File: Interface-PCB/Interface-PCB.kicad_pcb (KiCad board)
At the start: 2 copper layers, 36 parts, among them IC1 SN74LVC245AN, J10 LEVEL_SENSOR, J11 LEVEL_SENSOR, J12 LEVEL_SENSOR, J13 TEMPERATURE_SENSOR, J14 TEMPERATURE_SENSOR, J3 RASPBERRYPI-40-PIN-GPIO, J4 I2C_HEADER, J5 CONN_05JST, J6 CONN_05JST, J7 LEVEL_SENSOR, J8 LEVEL_SENSOR, J9 LEVEL_SENSOR, Q1 2N3904, Q10 2N3904, Q2 2N3904, Q3 2N3904, Q4 2N3904, Q5 2N3904, Q6 2N3904, Q7 2N3904, Q8 2N3904, Q9 2N3904, U3 CD74HC4067_MUX

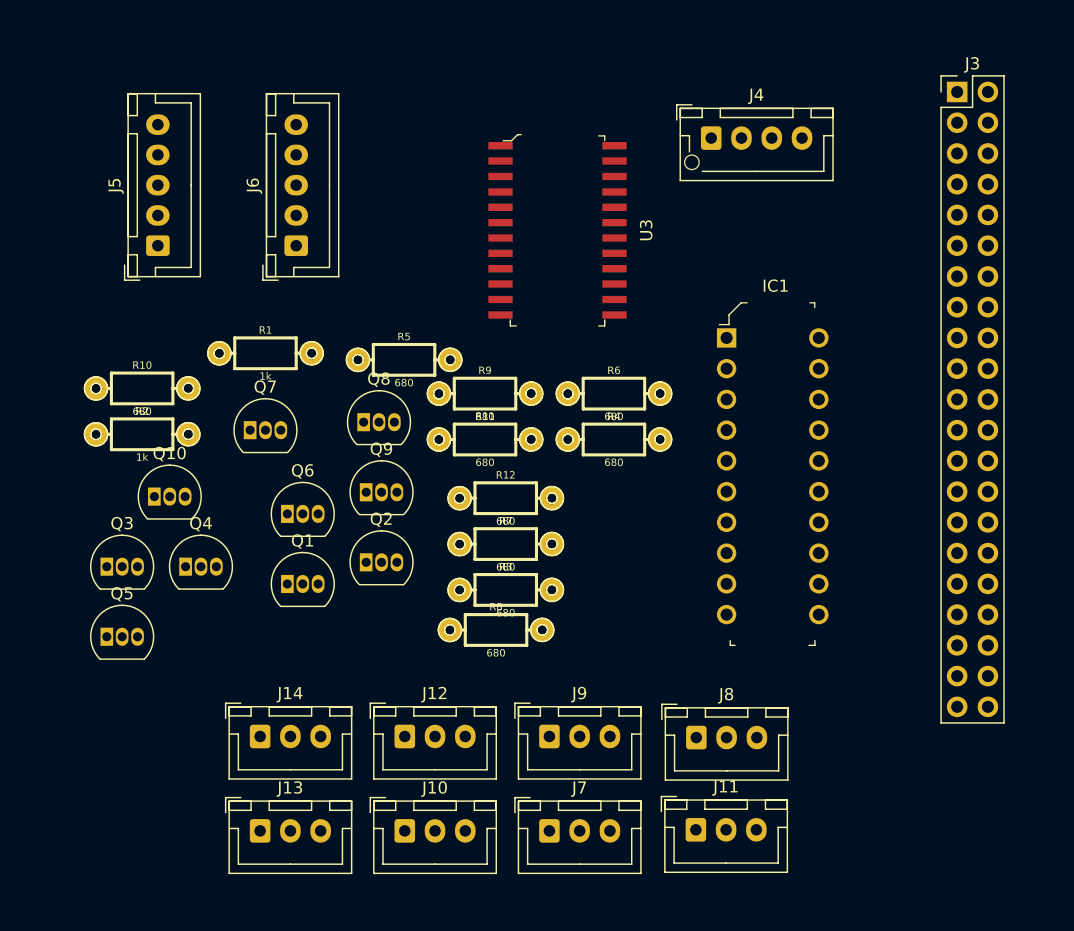
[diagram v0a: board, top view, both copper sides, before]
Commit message: Assign misc footprints for FDP
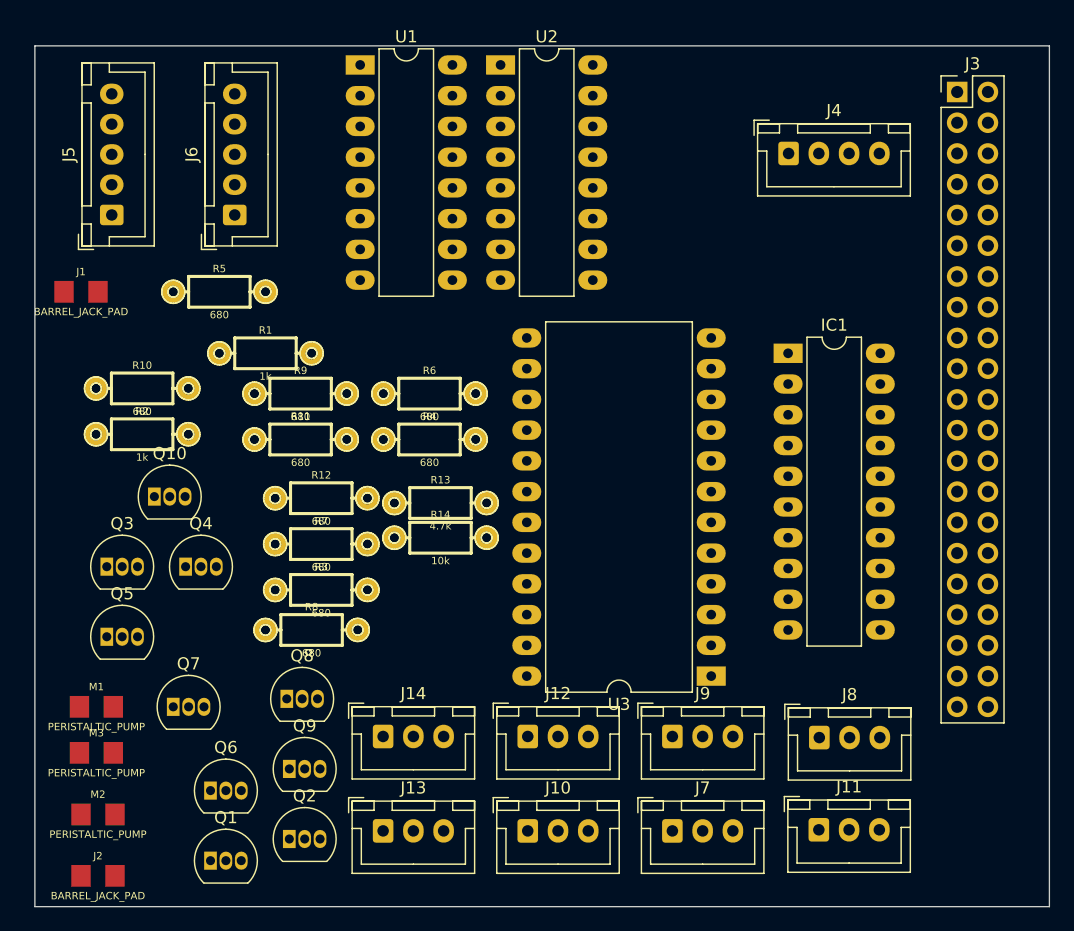
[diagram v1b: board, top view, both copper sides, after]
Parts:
- added J1: BARREL_JACK_PAD, Fuses:1206, F.Cu at (125.7, 95.2)
- added J2: BARREL_JACK_PAD, Fuses:1206, F.Cu at (127.1, 143.5)
- added M1: PERISTALTIC_PUMP, Fuses:1206, F.Cu at (127.0, 129.5)
- added M2: PERISTALTIC_PUMP, Fuses:1206, F.Cu at (127.1, 138.4)
- added M3: PERISTALTIC_PUMP, Fuses:1206, F.Cu at (127.0, 133.3)
- added R13: 4.7k, Resistors:AXIAL-0.3-KIT, F.Cu at (155.4, 112.7)
- added R14: 10k, Resistors:AXIAL-0.3-KIT, F.Cu at (155.4, 115.6)
- added U1: TB6612FNG_BREAKOUT, Package_DIP:DIP-16_W7.62mm_LongPads, F.Cu at (148.8, 76.5)
- added U2: TB6612FNG_BREAKOUT, Package_DIP:DIP-16_W7.62mm_LongPads, F.Cu at (160.4, 76.5)
- IC1: footprint digikey-footprints:DIP-20_W7.62mm -> Package_DIP:DIP-20_W7.62mm_LongPads
- J4: footprint Connector_JST:JST_XH_B4B-XH-AM_1x04_P2.50mm_Vertical -> Connector_JST:JST_XH_B4B-XH-A_1x04_P2.50mm_Vertical
- U3: footprint digikey-footprints:SOIC-24_W7.50mm -> Package_DIP:DIP-24_W15.24mm_LongPads
- moved U3 39.0 mm to (177.8, 127.0), turned to 180 degrees
- moved Q2 23.7 mm to (142.9, 140.5)
- moved Q6 23.7 mm to (136.4, 136.5)
- moved Q8 23.7 mm to (142.7, 128.9)
- moved Q1 23.7 mm to (136.4, 142.2)
- moved Q7 23.7 mm to (133.3, 129.5)
- moved Q9 23.7 mm to (142.9, 134.7)
- moved R5 16.3 mm to (137.2, 95.2)
- moved R12 15.2 mm to (145.6, 112.3)
- moved R3 15.2 mm to (145.6, 119.9)
- moved R4 15.2 mm to (154.5, 107.5)
- moved R6 15.2 mm to (154.5, 103.7)
- moved R7 15.2 mm to (145.6, 116.1)
- moved R8 15.2 mm to (144.8, 123.2)
- moved R11 15.2 mm to (143.9, 107.5)
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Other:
- board outline added: 83.8 x 71.1 mm

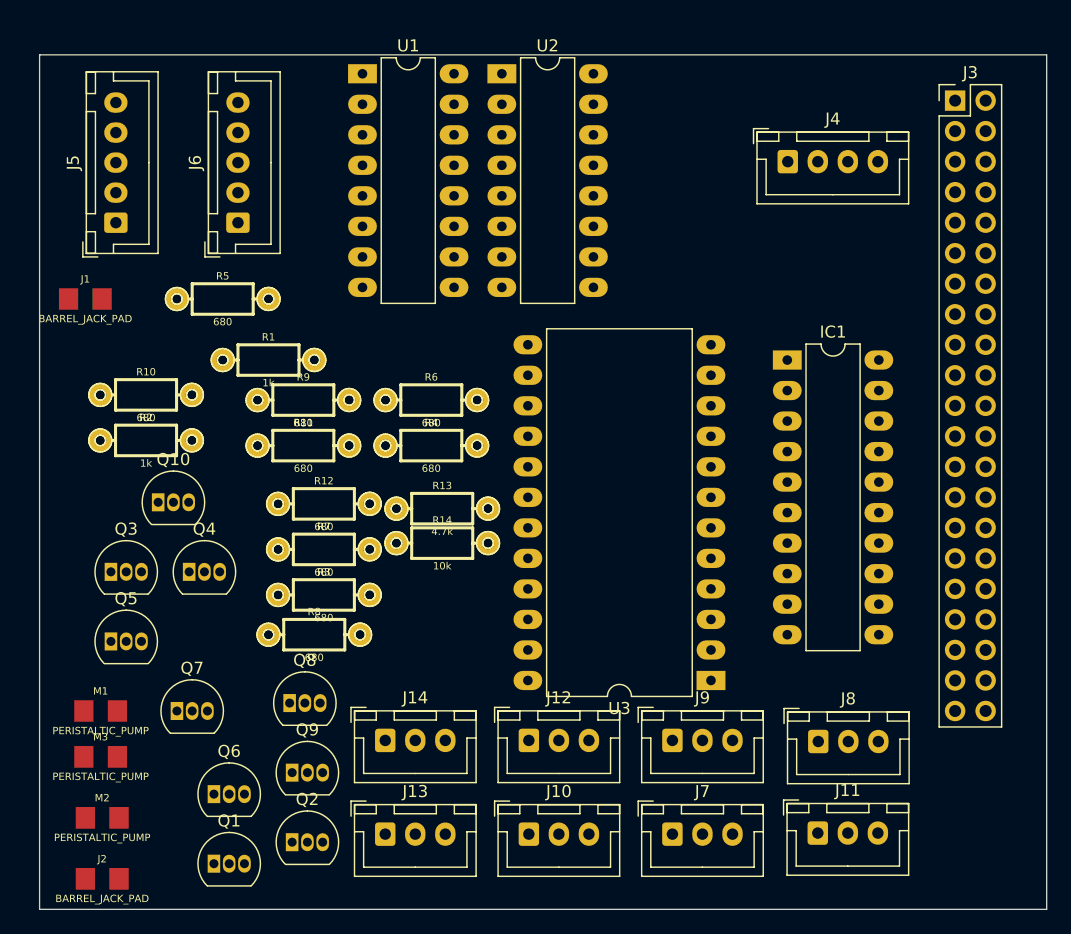
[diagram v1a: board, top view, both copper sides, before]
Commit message: Change to Highside switch
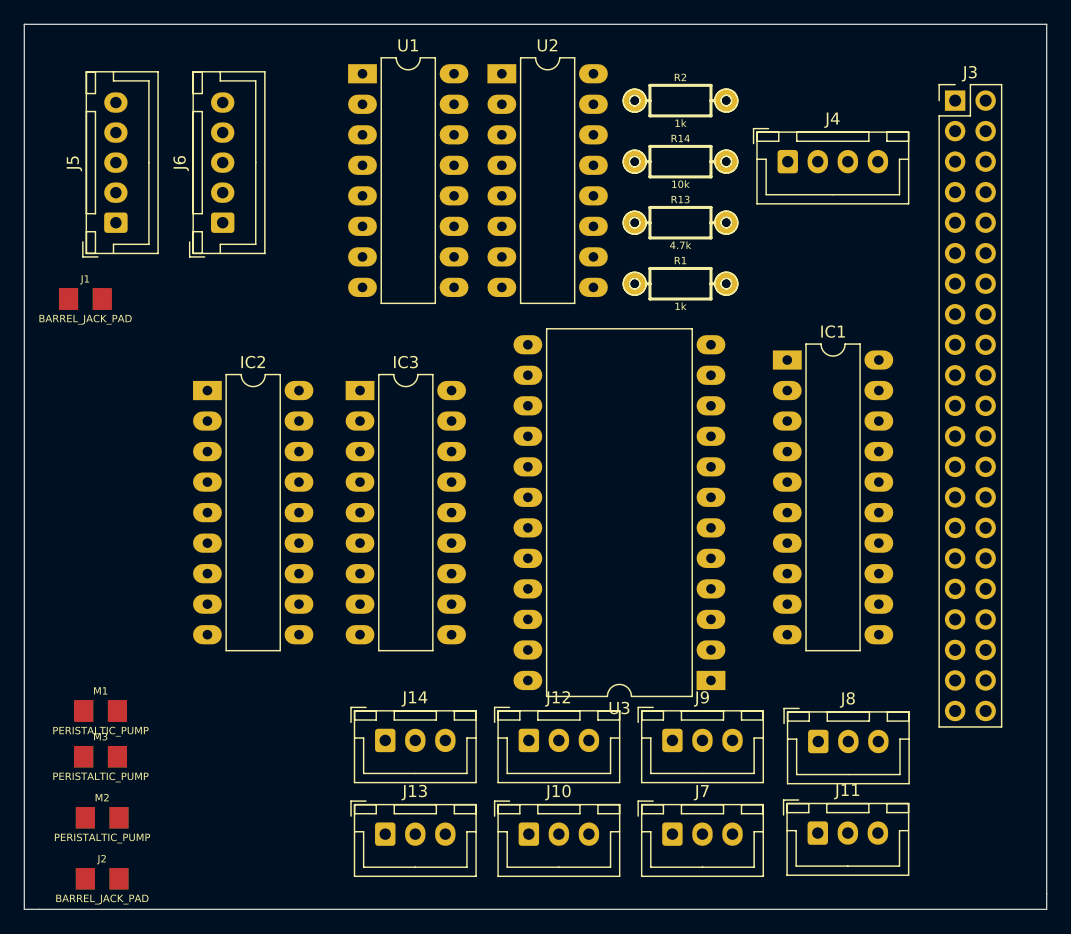
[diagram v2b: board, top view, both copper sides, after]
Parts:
- removed Q1, Q10, Q2, Q3, Q4, Q5, Q6, Q7, Q8, Q9: 2N3904, Package_TO_SOT_THT:TO-92_Inline
- removed R10, R11, R12, R3, R4, R5, R6, R7, R8, R9: 680, Resistors:AXIAL-0.3-KIT
- added IC2: TBD62783A, Package_DIP:DIP-18_W7.62mm_LongPads, F.Cu at (135.9, 102.9)
- added IC3: TBD62783A, Package_DIP:DIP-18_W7.62mm_LongPads, F.Cu at (148.6, 102.9)
- moved R2 52.7 mm to (175.3, 78.7)
- moved R14 37.4 mm to (175.3, 83.8)
- moved R1 34.9 mm to (175.3, 94.0)
- moved R13 31.0 mm to (175.3, 88.9)
- moved J6 1.27 mm to (137.2, 88.9)
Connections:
- J5 pad 1: OUT_1_ON -> Net-(IC2-Pad14)
- J5 pad 2: OUT_2_ON -> Net-(IC2-Pad15)
- J5 pad 3: OUT_3_ON -> Net-(IC2-Pad16)
- J5 pad 4: OUT_4_ON -> Net-(IC2-Pad17)
- J5 pad 5: OUT_5_ON -> Net-(IC2-Pad18)
- J6 pad 1: OUT_1_OFF -> Net-(IC3-Pad14)
- J6 pad 2: OUT_2_OFF -> Net-(IC3-Pad15)
- J6 pad 3: OUT_3_OFF -> Net-(IC3-Pad16)
- J6 pad 4: OUT_4_OFF -> Net-(IC3-Pad17)
- J6 pad 5: OUT_5_OFF -> Net-(IC3-Pad18)
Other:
- board size 83.8 x 71.1 mm -> 85.1 x 73.7 mm

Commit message: Review Schematic
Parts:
- R1, R2: value 1k -> 10k; footprint Resistors:AXIAL-0.3-KIT -> Resistor_THT:R_Axial_DIN0207_L6.3mm_D2.5mm_P10.16mm_Horizontal
- moved IC1 1.80 mm to (182.9, 101.6)
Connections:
- net Net-(J3-Pad12) renamed GPIO18
- net Net-(J3-Pad27) renamed ID_SD_UNUSED
- net Net-(J3-Pad28) renamed ID_SC_UNUSED
- net Net-(J3-Pad35) renamed GPIO19
- net Net-(J3-Pad37) renamed USER_LED_BUZZER
- IC1 pad 11: 3.3V -> Net-(IC1-Pad11)
- IC1 pad 12: 3.3V -> Net-(IC1-Pad12)
